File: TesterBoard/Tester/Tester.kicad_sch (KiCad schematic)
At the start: 110 parts, among them J1 Conn_01x03_Pin, J2 PJ-102A, J3 Conn_01x03_Pin, J4 Conn_01x02_Pin, J5 Conn_01x02_Pin, J6 Conn_01x02_Pin, J7 Conn_01x02_Pin, J8 Conn_01x16_Pin, J9 Conn_01x08_Pin, SW1 SW_Push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

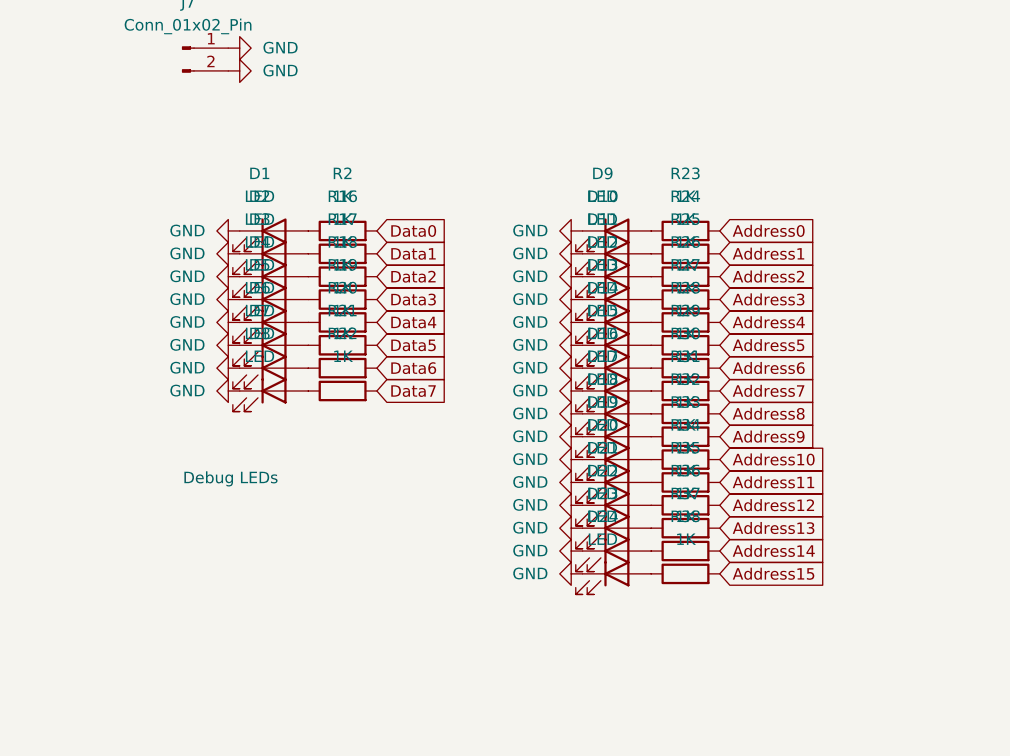
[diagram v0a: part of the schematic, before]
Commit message: updated PCB to fix logic, ready to place and route
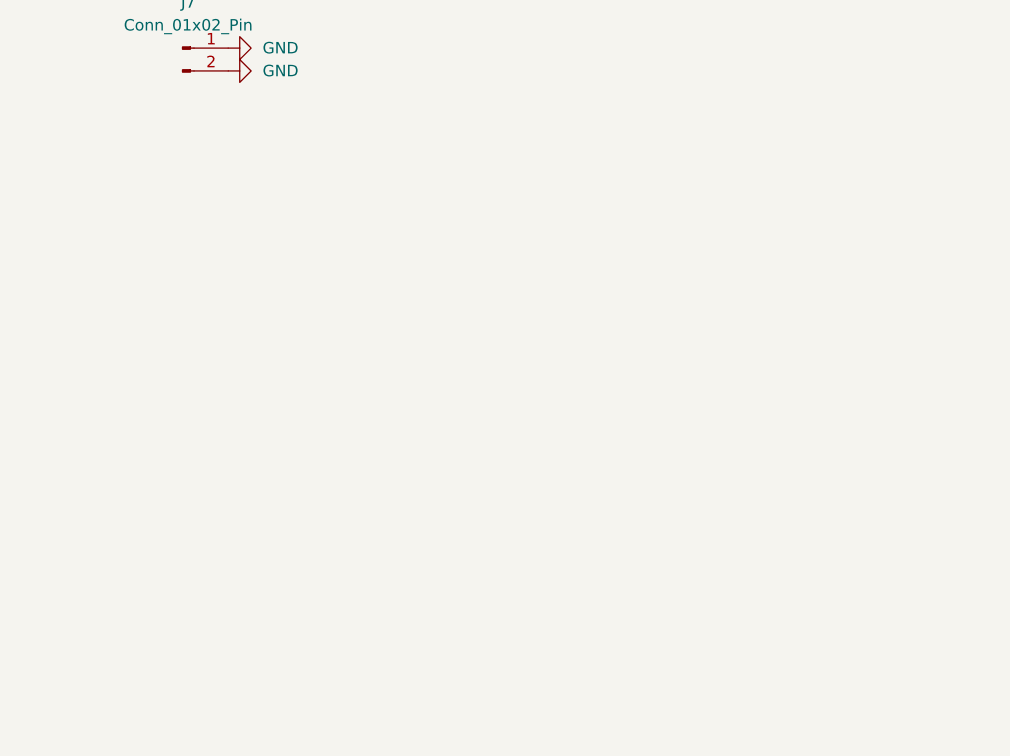
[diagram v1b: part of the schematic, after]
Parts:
- removed D1, D10, D11, D12, D13, D14, D15, D16, D17, D18, D19, D2, D20, D21, D22, D23, D24, D3, D4, D5, D6, D7, D8, D9: LED, ECE445L:LED_D5.0mm, symbol Device:LED
- removed R16, R17, R18, R19, R2, R20, R21, R22, R23, R24, R25, R26, R27, R28, R29, R30, R31, R32, R33, R34, R35, R36, R37, R38: 1K, ECE445L:R_Axial_DIN0204_L3.6mm_D1.6mm_P7.62mm_Horizontal, symbol Device:R
- J2: footprint Z80_Tester_Footprints:CUI_PJ-102A -> Connector_BarrelJack:BarrelJack_Horizontal
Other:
- note removed: "Debug LEDs"

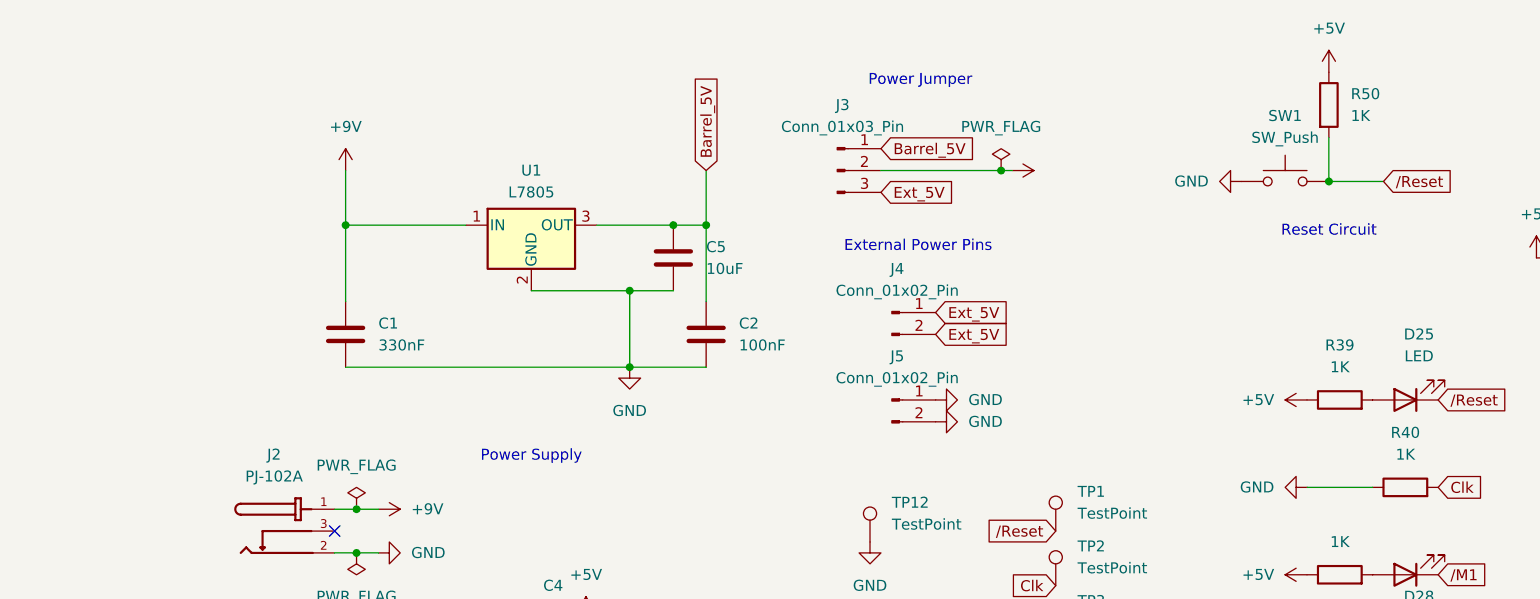
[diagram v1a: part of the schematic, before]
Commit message: minor changes to pcb : labels for schematic
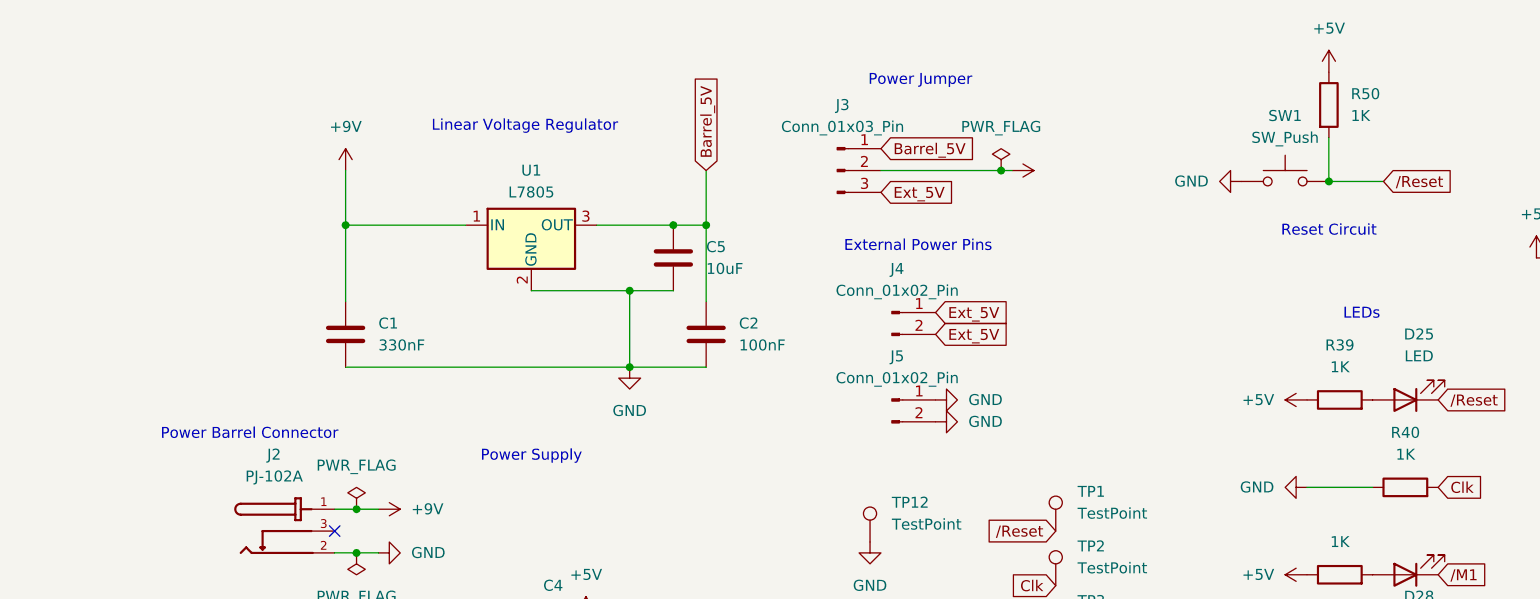
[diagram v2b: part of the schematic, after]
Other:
- note added: "LEDs"
- note added: "Linear Voltage Regulator"
- note added: "Power Barrel Connector"
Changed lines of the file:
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@@
+		)
+	)
+	(text "Power Barrel Connector"
+		(exclude_from_sim no)
+		(at 26.924 67.564 0)
+		(effects
+			(font
+				(size 1.27 1.27)
+			)
 		)
 	)
@@
 		(exclude_from_sim no)
 		(at 192.786 189.738 0)
+		(effects
+			(font
+				(size 1.27 1.27)
+			)
+		)
+	)
+	(text "Linear Voltage Regulator"
+		(exclude_from_sim no)
+		(at 58.928 31.75 0)
 		(effects
 			(font
@@
 		(effects
 			(font
+				(size 1.27 1.27)
+			)
+		)
+	)
+	(text "LEDs"
+		(exclude_from_sim no)
+		(at 156.21 53.594 0)
+		(effects
+			(font

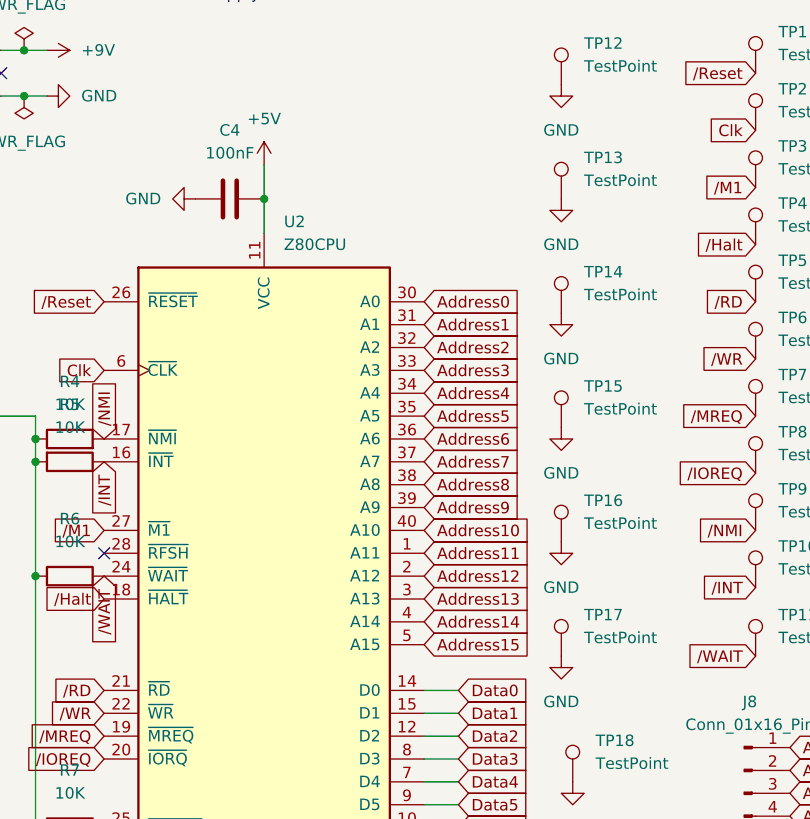
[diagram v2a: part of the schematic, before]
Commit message: Placed PCB awaiting review
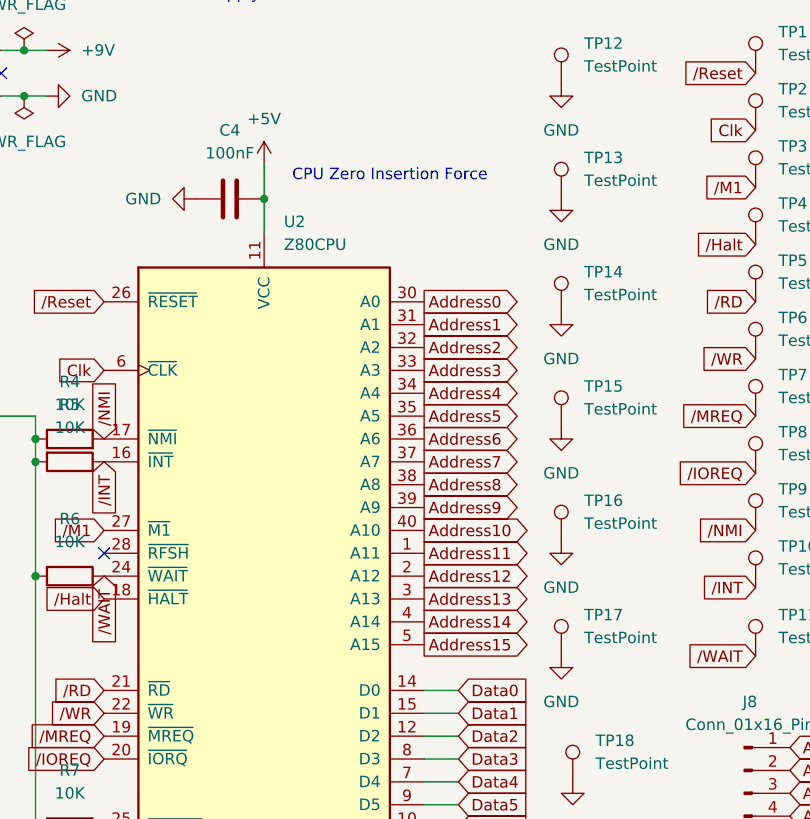
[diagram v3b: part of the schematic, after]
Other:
- note added: "CPU Zero Insertion Force"
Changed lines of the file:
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@@
+		)
+	)
+	(text "CPU Zero Insertion Force\n"
+		(exclude_from_sim no)
+		(at 80.01 90.17 0)
+		(effects
+			(font
+				(size 1.27 1.27)
+			)
 		)
 	)
@@
 	)
 	(global_label "Address12"
-		(shape input)
+		(shape output)
 		(at 83.82 134.62 0)
 		(fields_autoplaced yes)
@@
 	)
 	(global_label "Address10"
-		(shape input)
+		(shape output)
 		(at 83.82 129.54 0)
 		(fields_autoplaced yes)
@@
 	)
 	(global_label "Address14"
-		(shape input)
+		(shape output)
 		(at 83.82 139.7 0)
 		(fields_autoplaced yes)
@@
 	)
 	(global_label "Address0"
-		(shape input)
+		(shape output)
 		(at 83.82 104.14 0)
 		(fields_autoplaced yes)
@@
 	)
 	(global_label "Address9"
-		(shape input)
+		(shape output)
 		(at 83.82 127 0)
 		(fields_autoplaced yes)
@@
 	)
 	(global_label "Address15"
-		(shape input)
+		(shape output)
 		(at 83.82 142.24 0)
 		(fields_autoplaced yes)
@@
 	)
 	(global_label "Address4"
-		(shape input)
+		(shape output)
 		(at 83.82 114.3 0)
 		(fields_autoplaced yes)
@@
 	)
 	(global_label "Address8"
-		(shape input)
+		(shape output)
 		(at 83.82 124.46 0)
 		(fields_autoplaced yes)
@@
 	)
 	(global_label "Address13"
-		(shape input)
+		(shape output)
 		(at 83.82 137.16 0)
 		(fields_autoplaced yes)
@@
 	)
 	(global_label "Address1"
-		(shape input)
+		(shape output)
 		(at 83.82 106.68 0)
 		(fields_autoplaced yes)
@@
 	)
 	(global_label "Address7"
-		(shape input)
+		(shape output)
 		(at 83.82 121.92 0)
 		(fields_autoplaced yes)
@@
 	)
 	(global_label "Address6"
-		(shape input)
+		(shape output)
 		(at 83.82 119.38 0)
 		(fields_autoplaced yes)
@@
 	)
 	(global_label "Address2"
-		(shape input)
+		(shape output)
 		(at 83.82 109.22 0)
 		(fields_autoplaced yes)
@@
 	)
 	(global_label "Address3"
-		(shape input)
+		(shape output)
 		(at 83.82 111.76 0)
 		(fields_autoplaced yes)
@@
 	)
 	(global_label "Address5"
-		(shape input)
+		(shape output)
 		(at 83.82 116.84 0)
 		(fields_autoplaced yes)
@@
 	)
 	(global_label "Address11"
-		(shape input)
+		(shape output)
 		(at 83.82 132.08 0)
 		(fields_autoplaced yes)

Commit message: Almost done routing
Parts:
- added H1, H2, H3, H4: ~, ECE445L:MountingHole_4_40, symbol ECE445L:MountingHole
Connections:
- no-connect marks 3 -> 7
